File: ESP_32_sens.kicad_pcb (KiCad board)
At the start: 4 copper layers, 77 x 51.2 mm, 59 parts, among them J3 USB_C_Receptacle_USB2.0_16P, J4 Conn_01x04_Pin, SW1 SW_Push, U1 ESP32-S3, U2 MX25L6433FM2I-08G, U3 ESP-PSRAM32, U4 BMI323, U5 HT7533-1, U6 USBLC6-2SC6, U7 TLV62569DBV, Y1 Crystal_GND24

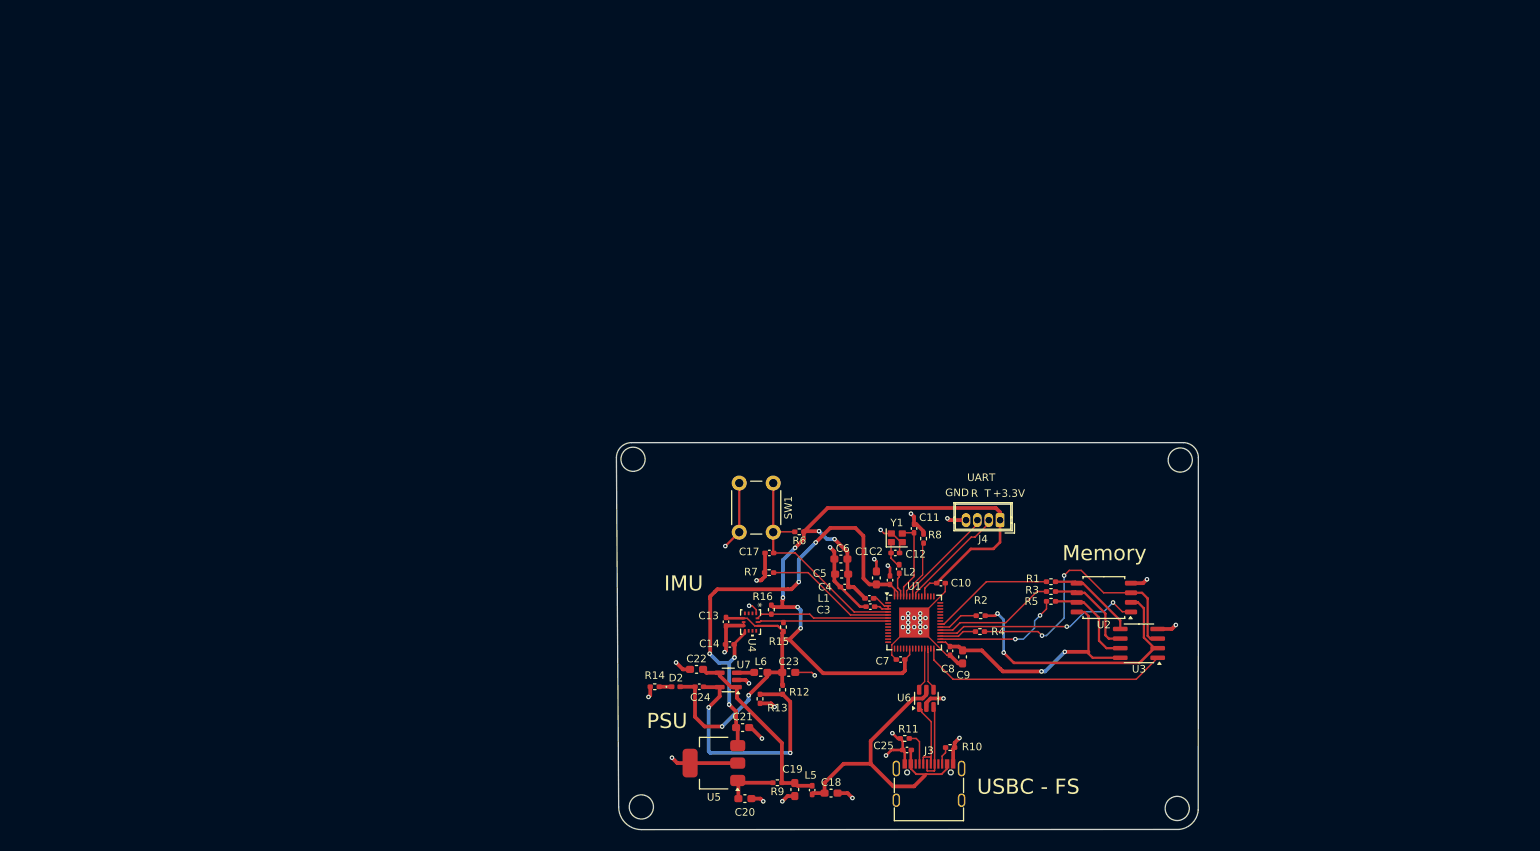
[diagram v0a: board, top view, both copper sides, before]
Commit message: Added antenna design
added pcb antenna design
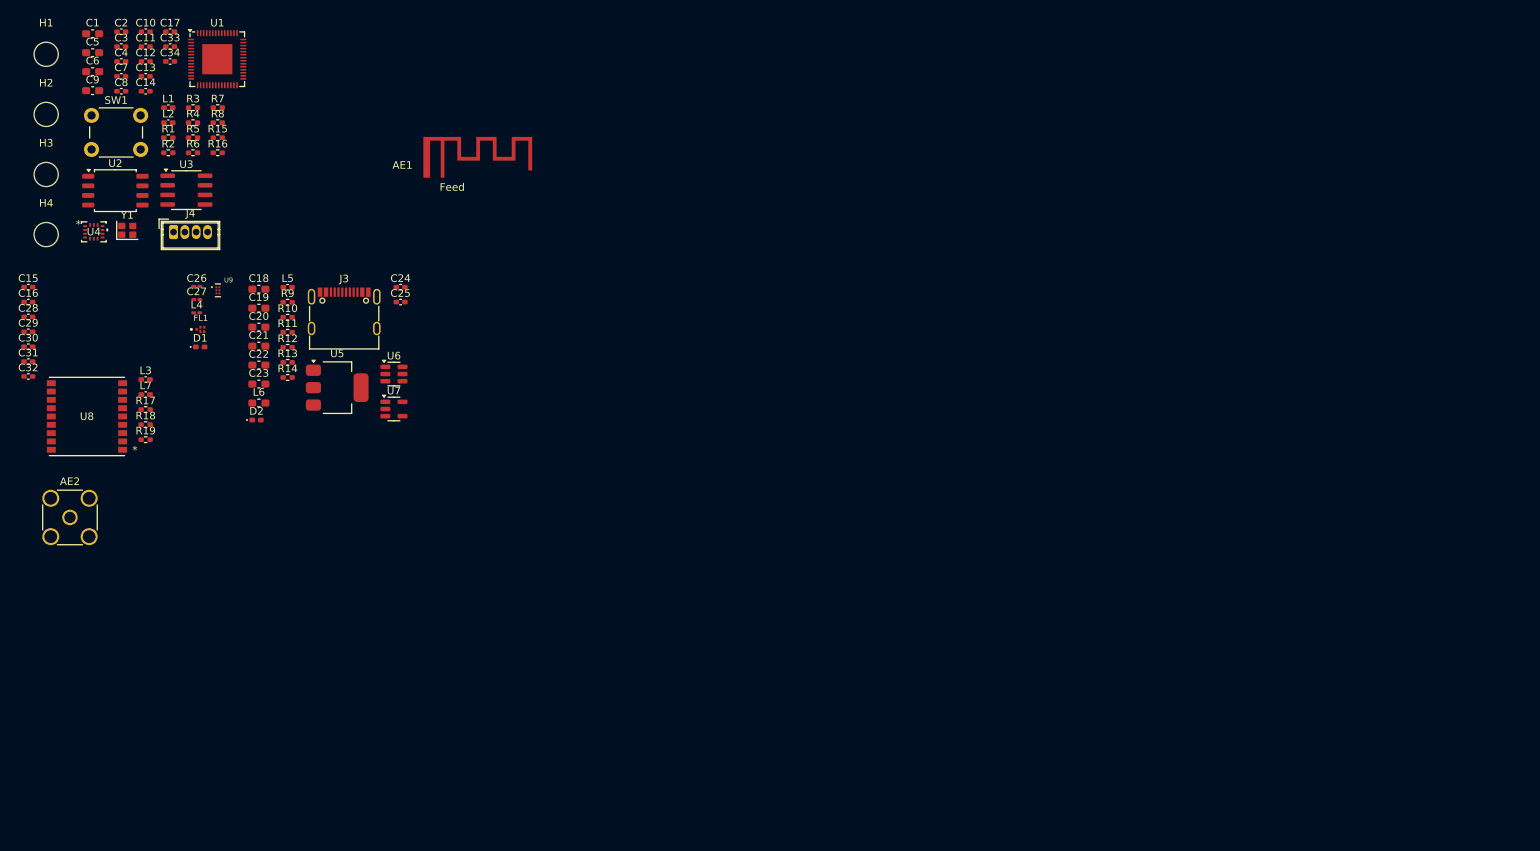
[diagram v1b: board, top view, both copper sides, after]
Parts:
- added AE1: Antenna_Chip, RF_extra:IFA_2.45_TI, F.Cu at (68.8, 41.6)
- added AE2: GNSS_ANT, Connector_Coaxial:SMA_Amphenol_132291-12_Vertical, F.Cu at (25.6, 83.8)
- added C15: 56p, Capacitor_SMD:C_0402_1005Metric_Pad0.74x0.62mm_HandSolder, F.Cu at (20.1, 53.3)
- added C16: 10n, Capacitor_SMD:C_0402_1005Metric_Pad0.74x0.62mm_HandSolder, F.Cu at (20.1, 55.3)
- added C26: 5.733p, Capacitor_SMD:C_0201_0603Metric_Pad0.64x0.40mm_HandSolder, F.Cu at (42.4, 53.2)
- added C27: 4.244p, Capacitor_SMD:C_0201_0603Metric_Pad0.64x0.40mm_HandSolder, F.Cu at (42.4, 55.0)
- added C28: 56p, Capacitor_SMD:C_0402_1005Metric_Pad0.74x0.62mm_HandSolder, F.Cu at (20.1, 57.3)
- added C29: 56p, Capacitor_SMD:C_0402_1005Metric_Pad0.74x0.62mm_HandSolder, F.Cu at (20.1, 59.2)
- added C30: 56p, Capacitor_SMD:C_0402_1005Metric_Pad0.74x0.62mm_HandSolder, F.Cu at (20.1, 61.2)
- added C31: 56p, Capacitor_SMD:C_0402_1005Metric_Pad0.74x0.62mm_HandSolder, F.Cu at (20.1, 63.2)
- added C32: 120p, Capacitor_SMD:C_0402_1005Metric_Pad0.74x0.62mm_HandSolder, F.Cu at (20.1, 65.2)
- added C33: 56p, Capacitor_SMD:C_0402_1005Metric_Pad0.74x0.62mm_HandSolder, F.Cu at (38.9, 21.5)
- added C34: 56p, Capacitor_SMD:C_0402_1005Metric_Pad0.74x0.62mm_HandSolder, F.Cu at (38.9, 23.5)
- added D1: D_TVS, Diode_SMD:D_0402_1005Metric_Pad0.77x0.64mm_HandSolder, F.Cu at (42.8, 61.2)
- added FL1: B39162B4327P810, RF:FIL_B39162B4327P810, F.Cu at (42.9, 58.9)
- added L3: 27n, Inductor_SMD:L_0402_1005Metric_Pad0.77x0.64mm_HandSolder, F.Cu at (35.6, 65.5)
- added L4: 1.696n, Inductor_SMD:L_0201_0603Metric_Pad0.64x0.40mm_HandSolder, F.Cu at (42.4, 56.7)
- added L7: 5.6n, Inductor_SMD:L_0402_1005Metric_Pad0.77x0.64mm_HandSolder, F.Cu at (35.6, 67.5)
- added R17: 10K, Resistor_SMD:R_0402_1005Metric_Pad0.72x0.64mm_HandSolder, F.Cu at (35.6, 69.5)
- added R18: 1.5k, Resistor_SMD:R_0402_1005Metric_Pad0.72x0.64mm_HandSolder, F.Cu at (35.6, 71.5)
- added R19: 1.5k, Resistor_SMD:R_0402_1005Metric_Pad0.72x0.64mm_HandSolder, F.Cu at (35.6, 73.5)
- added U8: TESEO-LIV3R, RF:ARRAY_LIV3R_STM, F.Cu at (27.8, 70.4)
- added U9: BGA725L6E6327FTSA1, RF:AMP_BGA725L6E6327FTSA1, F.Cu at (45.2, 53.8)
- moved H4 167.8 mm to (22.5, 46.4)
- moved H3 154.7 mm to (22.5, 38.4)
- moved U2 141.4 mm to (31.6, 40.6), turned to 0 degrees
- moved U3 139.6 mm to (41.0, 40.5), turned to 0 degrees
- moved C9 137.3 mm to (28.6, 27.3), turned to 0 degrees
- moved C8 132.3 mm to (32.4, 27.4), turned to 0 degrees
- moved R1 130.7 mm to (38.6, 33.6)
- moved R3 130.3 mm to (41.9, 29.6)
- moved R5 129.0 mm to (41.9, 33.6)
- moved C7 128.8 mm to (32.4, 25.4), turned to 0 degrees
- moved C10 128.0 mm to (35.6, 19.5)
- moved H1 127.0 mm to (22.5, 22.5)
- moved C1 126.2 mm to (28.6, 19.8), turned to 0 degrees
- moved C2 124.9 mm to (32.4, 19.5), turned to 0 degrees
- moved R4 124.0 mm to (41.9, 31.6)
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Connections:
- U1 pad 1: unconnected-(U1-LNA_IN-Pad1) -> RF_IN
- U1 pad 11: unconnected-(U1-GPIO6-Pad11) -> I2C_SDA_2
- U1 pad 12: unconnected-(U1-GPIO7-Pad12) -> I2C_SCL_2
- U1 pad 13: unconnected-(U1-GPIO8-Pad13) -> UART2_RX
- U1 pad 14: unconnected-(U1-GPIO9-Pad14) -> UART2_TX
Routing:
- net +3.3V: track 137.8 -> 0.00 mm, vias 8 -> 0
- net GND: track 115.0 -> 0.00 mm, vias 42 -> 0
- net +3.3VA: track 66.8 -> 0.00 mm, vias 5 -> 0
- net VBUS: track 41.6 -> 0.00 mm
- net SPIQ: track 37.3 -> 0.00 mm, vias 2 -> 0
- net SPIWP: track 36.7 -> 0.00 mm, vias 2 -> 0
- net VDD_SPI: track 33.5 -> 0.00 mm, vias 2 -> 0
- net SPICS1: track 33.4 -> 0.00 mm
- net /PSU/BUCK_FB: track 33.3 -> 0.00 mm, vias 2 -> 0
- net /MCU/Chip_pu: track 30.5 -> 0.00 mm
- net SPICS0: track 27.4 -> 0.00 mm, vias 2 -> 0
- net +5V: track 25.0 -> 0.00 mm
- net I2C_SDA: track 17.7 -> 0.00 mm
- net Net-(U1-GPIO0): track 17.5 -> 0.00 mm
- net I2C_SCL: track 17.3 -> 0.00 mm
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- removed copper zone on In1.Cu, net GND
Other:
- board outline removed
- board text removed: "+3.3V"
- board text removed: "Flatrim Dreshaj AMNTL - Scan Motion Controller V1 8/14/2025"
- board text removed: "GND"
- board text removed: "IMU"
- board text removed: "Memory"
- board text removed: "PSU"
- board text removed: "R"
- board text removed: "T"
- board text removed: "UART"
- board text removed: "USBC - FS"

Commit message: placement done
placement done, routing left
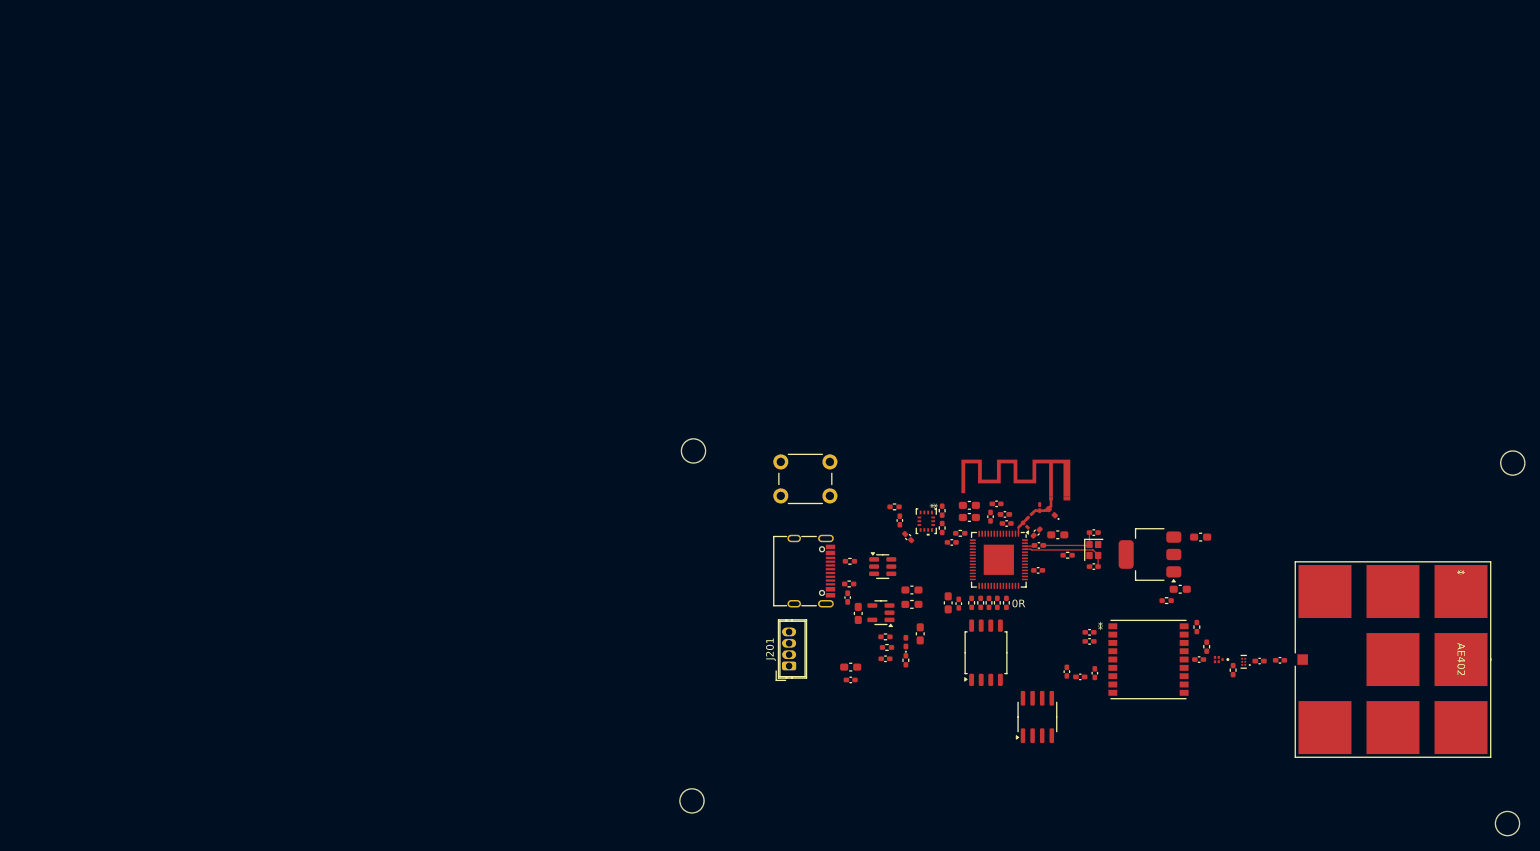
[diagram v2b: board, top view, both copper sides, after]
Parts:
- removed C29, C33, C34: 56p, Capacitor_SMD:C_0402_1005Metric_Pad0.74x0.62mm_HandSolder
- AE402: renamed from AE2; footprint Connector_Coaxial:SMA_Amphenol_132291-12_Vertical -> RF_Antenna:SGGP.25.4.A.02_TAL
- moved H202 214.9 mm to (215.8, 124.3)
- moved H203 197.8 mm to (216.5, 76.6)
- moved AE402 176.1 mm to (200.6, 102.6), turned to -90 degrees
- moved C408 169.8 mm to (185.7, 102.7), turned to 180 degrees
- moved C409 159.8 mm to (175.0, 102.6), turned to 180 degrees
- moved L403 151.5 mm to (183.0, 102.8), turned to 180 degrees
- moved C407 150.1 mm to (161.2, 104.4), turned to 90 degrees
- moved R403 148.0 mm to (179.5, 104.0), turned to 90 degrees
- moved C404 146.8 mm to (160.5, 100.2)
- moved C403 145.8 mm to (157.5, 104.2), turned to 90 degrees
- moved C406 145.4 mm to (160.5, 99.0)
- moved U402 144.3 mm to (180.9, 102.9), turned to 180 degrees
- moved U401 144.1 mm to (168.3, 102.6), turned to 180 degrees
- moved C209 143.9 mm to (156.3, 86.1)
- moved C205 143.1 mm to (161.1, 90.3), turned to 180 degrees
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- renumbered AE1 to AE401, C13 to C201, C14 to C204, C11 to C205, C6 to C206, C12 to C207, C5 to C208, C1 to C209, C4 to C210, C2 to C211, C3 to C212, C8 to C213, C7 to C214, C10 to C215, C9 to C216, C17 to C217, C18 to C301, C25 to C302, C19 to C303, C20 to C304, C22 to C305, C21 to C306, C23 to C307, C24 to C308, C26 to C402, C16 to C403, C28 to C404, C27 to C405, C30 to C406, C15 to C407, C32 to C408, C31 to C409, D2 to D301, D1 to D401, FL1 to FL401, H1 to H201, H2 to H202, H3 to H203, H4 to H204, J4 to J201, J3 to J301, L2 to L201, L1 to L202, L5 to L301, L6 to L302, L3 to L401, L4 to L402, L7 to L403, R16 to R201, R15 to R202, R7 to R203, R5 to R204, R4 to R205, R3 to R206, R2 to R207, R1 to R208, R8 to R209, R6 to R210, R11 to R301, R10 to R302, R9 to R303, R12 to R304, R13 to R305, R14 to R306, R18 to R401, R19 to R402, R17 to R403, SW1 to SW201, U4 to U201, U1 to U202, U2 to U203, U3 to U204, U6 to U301, U5 to U302, U7 to U303, U8 to U401, U9 to U402, Y1 to Y201
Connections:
- net /MCU/Chip_pu renamed /MCU [2]/Chip_pu
- net /MCU/XTAL_N renamed /MCU [2]/XTAL_N
- net /MCU/XTAL_P renamed /MCU [2]/XTAL_P
- net /MCU/vdd_3p3 in renamed /MCU [2]/vdd_3p3 in
- net /PSU/+5V_FILT renamed /PSU [3]/+5V_FILT
- net /PSU/BUCK_FB renamed /PSU [3]/BUCK_FB
- net /PSU/BUCK_SW renamed /PSU [3]/BUCK_SW
- net /PSU/CC_1_pulldown renamed /PSU [3]/CC_1_pulldown
- net /PSU/CC_2_pulldown renamed /PSU [3]/CC_2_pulldown
- net /PSU/LED_PWR_K renamed /PSU [3]/LED_PWR_K
- net /PSU/usbc_d+ renamed /PSU [3]/usbc_d+
- net /PSU/usbc_d- renamed /PSU [3]/usbc_d-
- net /RF/ANTOFF renamed /RF [4]/ANTOFF
- net Net-(U8-VBATT) renamed /RF [4]/GPS_VCC
- AE401 pad 1: feed -> /RF [4]/feed_pin
- C405 pad 1: Net-(AE1-PCB_Trace) -> /RF [4]/feed_pin
- D401 pad 2: Net-(AE1-PCB_Trace) -> /RF [4]/feed_pin
- L402 pad 2: Net-(AE1-PCB_Trace) -> /RF [4]/feed_pin
- U202 pad 11: I2C_SDA_2 -> unconnected-(U202-GPIO6-Pad11)
- U202 pad 12: I2C_SCL_2 -> unconnected-(U202-GPIO7-Pad12)
- U202 pad 13: UART2_RX -> unconnected-(U202-GPIO8-Pad13)
- U202 pad 14: UART2_TX -> unconnected-(U202-GPIO9-Pad14)
- U202 pad 40: unconnected-(U1-GPIO35-Pad40) -> UART2_TX
- U202 pad 41: unconnected-(U1-GPIO36-Pad41) -> UART2_RX
- U202 pad 42: unconnected-(U1-GPIO37-Pad42) -> I2C_SDA_2
- U202 pad 43: unconnected-(U1-GPIO38-Pad43) -> I2C_SCL_2
- U401 pad 4: PPS_GPS -> unconnected-(U401-1PPS-Pad4)
- U401 pad 5: WAKEUP_GPS -> unconnected-(U401-Wake-Up-Pad5)
- U401 pad 9: RESET_GPS -> unconnected-(U401-SYS_RSTn-Pad9)
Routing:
- net /MCU [2]/XTAL_N: track 0.00 -> 11.5 mm
- net Net-(C207-Pad1): track 0.00 -> 7.74 mm
- net /RF [4]/feed_pin: track 0.00 -> 3.88 mm
- net RF_IN: track 0.00 -> 2.56 mm
- net /MCU [2]/XTAL_P: track 0.00 -> 1.32 mm
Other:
- board text added: "0R"

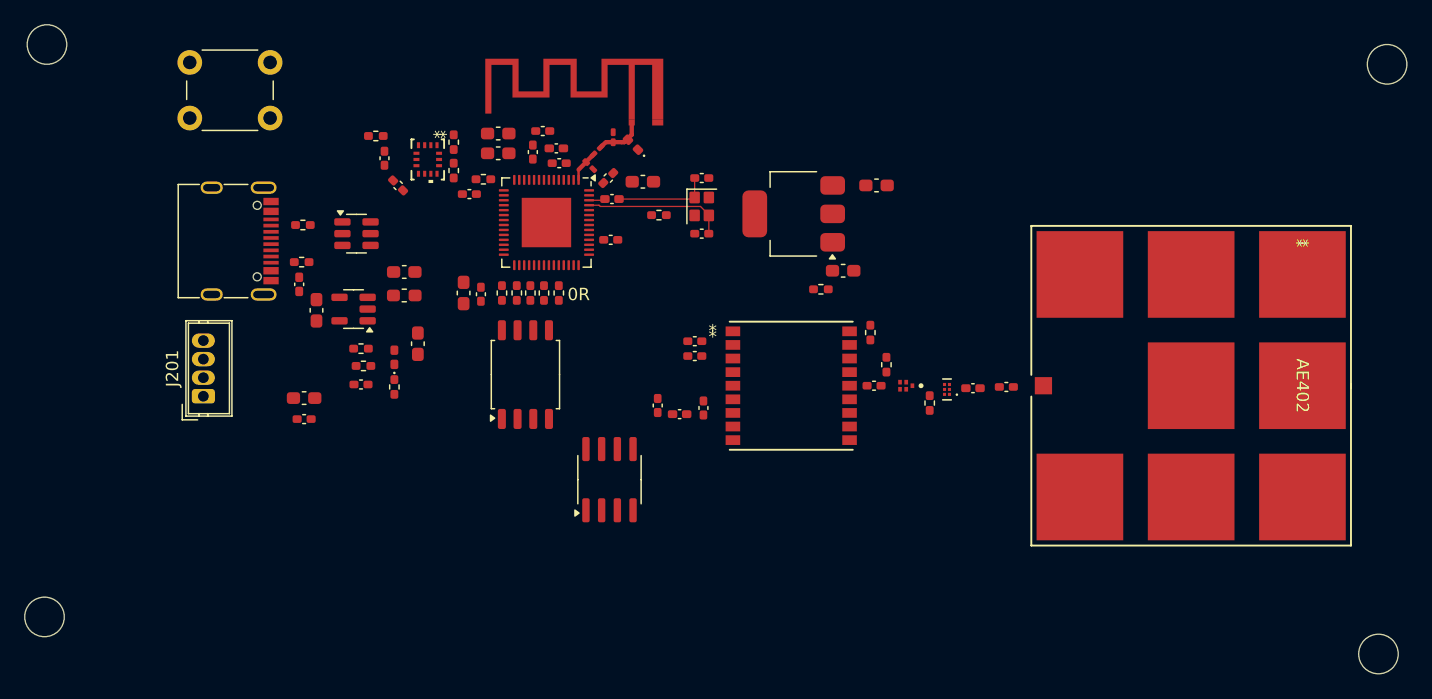
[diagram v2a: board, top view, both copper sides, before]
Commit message: added via stichitching and routing,
routing mostly done, Only power left
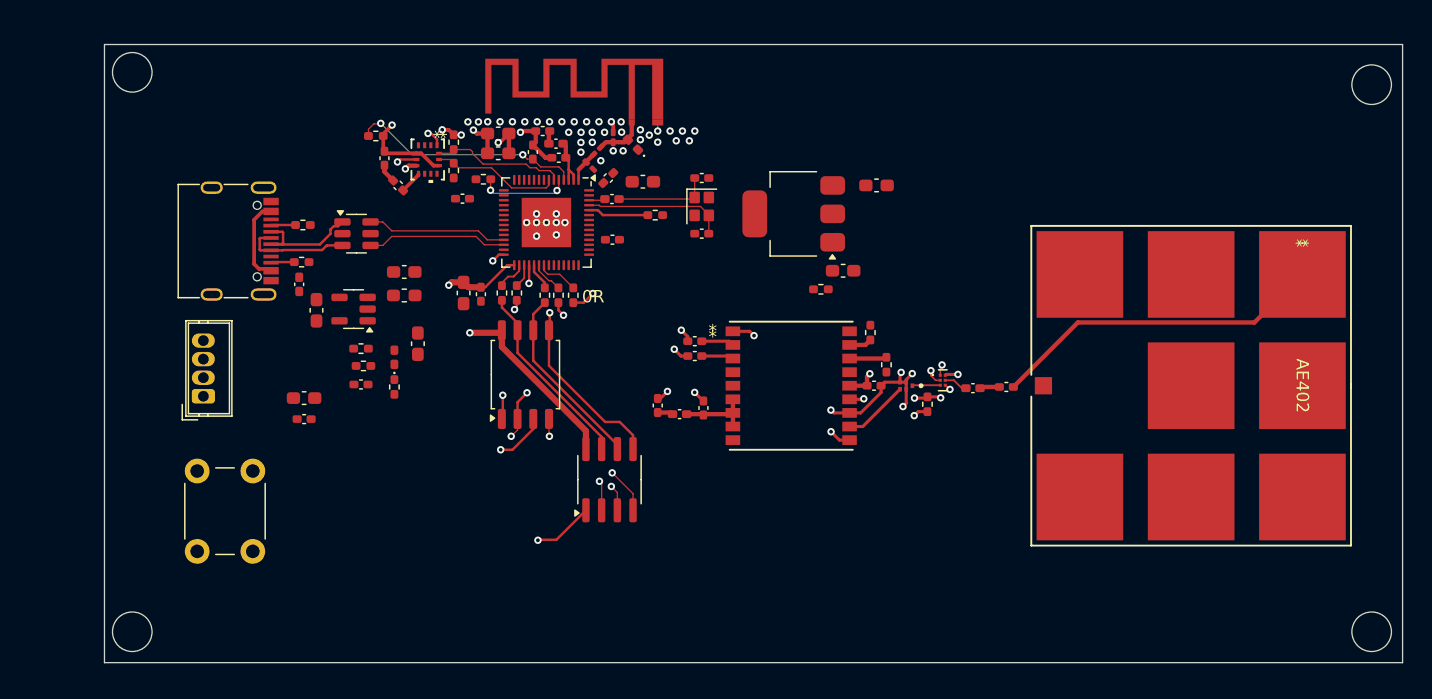
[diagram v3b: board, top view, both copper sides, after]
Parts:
- moved H201 48.0 mm to (115.0, 122.5)
- moved H204 44.6 mm to (115.0, 77.2)
- moved SW201 39.6 mm to (120.2, 116.0), turned to 90 degrees
- moved H203 2.07 mm to (215.2, 78.2)
- moved H202 1.88 mm to (215.2, 122.5)
- moved R206 1.18 mm to (148.4, 95.3)
- moved R207 1.18 mm to (149.5, 95.3)
- moved R208 1.18 mm to (150.7, 95.3)
- moved U402 0.81 mm to (180.6, 102.2), turned to 0 degrees
- moved C214 0.67 mm to (141.7, 87.5)
- moved C212 0.44 mm to (149.5, 84.2)
- moved L202 0.38 mm to (149.3, 83.0)
- moved R209 0.30 mm to (157.3, 88.8)
- moved R403 0.21 mm to (179.3, 104.1)
- moved C215 0.14 mm to (153.8, 90.8)
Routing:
- net GND: track 0.00 -> 49.4 mm, vias 0 -> 64
- net SPICS1: track 0.00 -> 36.0 mm, vias 0 -> 2
- net SPIWP: track 0.00 -> 29.7 mm, vias 0 -> 3
- net Net-(AE402-A): track 0.00 -> 27.2 mm
- net VDD_SPI: track 0.00 -> 26.0 mm, vias 0 -> 2
- net SPIQ: track 0.00 -> 23.8 mm, vias 0 -> 4
- net +3.3V: track 0.00 -> 21.6 mm, vias 0 -> 4
- net SPID: track 0.00 -> 21.3 mm, vias 0 -> 2
- net /MCU [2]/Chip_pu: track 0.00 -> 18.8 mm, vias 0 -> 2
- net SPIHD: track 0.00 -> 15.4 mm
- net SPICLK: track 0.00 -> 15.1 mm
- net SPICS0: track 0.00 -> 13.8 mm, vias 0 -> 2
- net USB_D-: track 0.00 -> 11.4 mm
- net /RF [4]/ANTOFF: track 0.00 -> 11.4 mm, vias 0 -> 4
- net USB_D+: track 0.00 -> 11.4 mm
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- added copper zone on In1.Cu, net GND
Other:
- board outline added: 105 x 50 mm
